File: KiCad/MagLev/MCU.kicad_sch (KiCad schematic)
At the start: 40 parts, among them J2 Programming header, J4 USB_B_Micro, Q16 TEMT7000X01, U6 ATmega328P-A, U8 FT232RL, U9 LM1117MP-5.0, Y3 J49SMH-16MHz

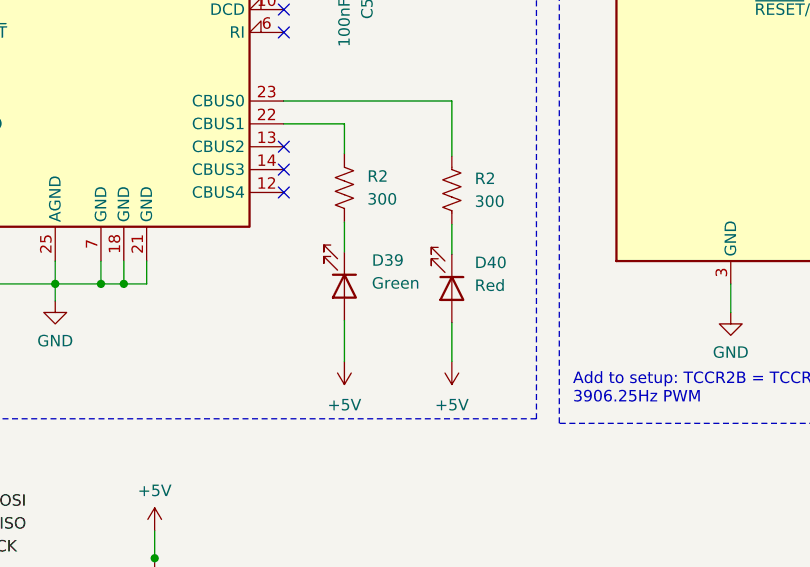
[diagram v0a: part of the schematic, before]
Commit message: Update BOM with JLCPCB PNs.
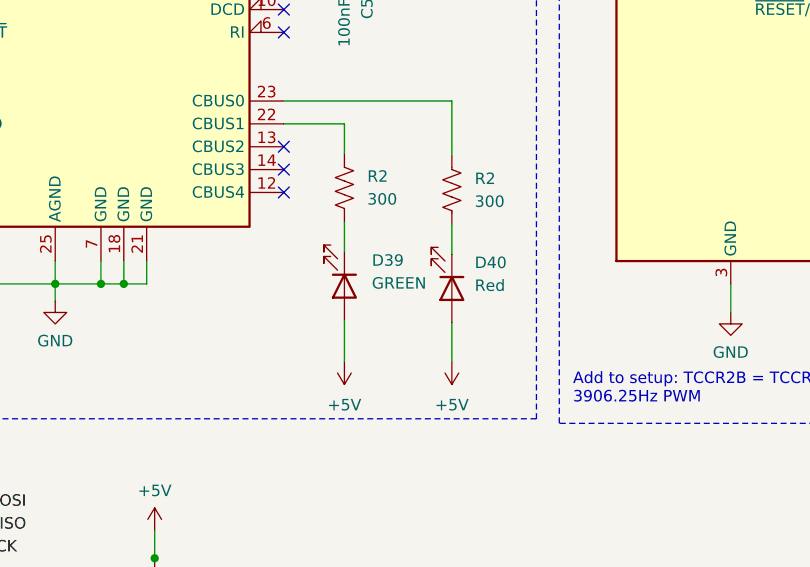
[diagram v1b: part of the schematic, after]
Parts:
- C5: JLC Part Number (none) -> C1804
- C5: JLC Part Number (none) -> C15850
- C5: JLC Part Number (none) -> C28233
- D28: JLC Part Number (none) -> C95872
- D39: value Green -> GREEN; JLC Part Number (none) -> C2297
- D40: JLC Part Number (none) -> C84256
- J2: JLC Part Number (none) -> C5142239
- J4: JLC Part Number (none) -> C428496
- R2: JLC Part Number (none) -> C17617
- R2: JLC Part Number (none) -> C17513
- R2: JLC Part Number (none) -> C17514
- R52: JLC Part Number (none) -> C3949945
- RESET1: JLC Part Number (none) -> C221877
- U6: JLC Part Number (none) -> C14877
- U8: JLC Part Number (none) -> C8690
- U9: JLC Part Number (none) -> C131933
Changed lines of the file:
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@@
       (effects (font (size 1.27 1.27)) hide)
     )
-    (property "JLC Part Number" "" (at 205.613 82.677 0)
+    (property "JLC Part Number" "C1804" (at 205.613 82.677 0)
       (effects (font (size 1.27 1.27)) hide)
     )
@@
       (effects (font (size 1.27 1.27)) hide)
     )
-    (property "JLC Part Number" "" (at 116.332 111.76 0)
+    (property "JLC Part Number" "C17617" (at 116.332 111.76 0)
       (effects (font (size 1.27 1.27)) hide)
     )
@@
       (effects (font (size 1.27 1.27)) hide)
     )
-    (property "JLC Part Number" "" (at 60.96 152.654 0)
+    (property "JLC Part Number" "C17513" (at 60.96 152.654 0)
       (effects (font (size 1.27 1.27)) hide)
     )
@@
       (effects (font (size 1.27 1.27)) hide)
     )
-    (property "JLC Part Number" "" (at 89.281 94.488 0)
+    (property "JLC Part Number" "C8690" (at 89.281 94.488 0)
       (effects (font (size 1.27 1.27)) hide)
     )
@@
       (effects (font (size 1.27 1.27)) hide)
     )
-    (property "JLC Part Number" "" (at 201.422 119.888 0)
+    (property "JLC Part Number" "C221877" (at 201.422 119.888 0)
       (effects (font (size 1.27 1.27)) hide)
     )
@@
       (effects (font (size 1.27 1.27)) hide)
     )
-    (property "JLC Part Number" "" (at 52.07 27.432 0)
+    (property "JLC Part Number" "C131933" (at 52.07 27.432 0)
       (effects (font (size 1.27 1.27)) hide)
     )
@@
       (effects (font (size 1.27 1.27)) hide)
     )
-    (property "JLC Part Number" "" (at 65.532 31.75 0)
+    (property "JLC Part Number" "C15850" (at 65.532 31.75 0)
       (effects (font (size 1.27 1.27)) hide)
     )
@@
       (effects (font (size 1.27 1.27)) hide)
     )
-    (property "JLC Part Number" "" (at 50.927 84.328 0)
+    (property "JLC Part Number" "C17513" (at 50.927 84.328 0)
       (effects (font (size 1.27 1.27)) hide)
     )
@@
       (effects (font (size 1.27 1.27)) hide)
     )
-    (property "JLC Part Number" "" (at 148.463 34.163 0)
+    (property "JLC Part Number" "C28233" (at 148.463 34.163 0)
       (effects (font (size 1.27 1.27)) hide)
     )
@@
       (effects (font (size 1.27 1.27)) hide)
     )
-    (property "JLC Part Number" "" (at 35.56 32.258 0)
+    (property "JLC Part Number" "C15850" (at 35.56 32.258 0)
       (effects (font (size 1.27 1.27)) hide)
     )
@@
       (effects (font (size 1.27 1.27)) hide)
     )
-    (property "JLC Part Number" "" (at 29.337 84.328 0)
+    (property "JLC Part Number" "C428496" (at 29.337 84.328 0)
       (effects (font (size 1.27 1.27)) hide)
     )
@@
       (effects (font (size 1.27 1.27)) hide)
     )
-    (property "JLC Part Number" "" (at 66.421 155.194 0)
+    (property "JLC Part Number" "C17513" (at 66.421 155.194 0)
       (effects (font (size 1.27 1.27)) hide)
     )
@@
       (effects (font (size 1.27 1.27)) hide)
     )
-    (property "JLC Part Number" "" (at 95.25 156.718 0)
+    (property "JLC Part Number" "C3949945" (at 95.25 156.718 0)
       (effects (font (size 1.27 1.27)) hide)
     )
@@
       (effects (font (size 1.27 1.27)) (justify left))
     )
-    (property "Value" "Green" (at 119.38 122.3645 90)
+    (property "Value" "GREEN" (at 119.38 122.3645 90)
       (effects (font (size 1.27 1.27)) (justify left))
     )
@@
       (effects (font (size 1.27 1.27)) hide)
     )
-    (property "JLC Part Number" "" (at 116.332 122.682 0)
+    (property "JLC Part Number" "C2297" (at 116.332 122.682 0)
       (effects (font (size 1.27 1.27)) hide)
     )
@@
       (effects (font (size 1.27 1.27)) hide)
     )
-    (property "JLC Part Number" "" (at 201.422 106.68 0)
+    (property "JLC Part Number" "C17513" (at 201.422 106.68 0)
       (effects (font (size 1.27 1.27)) hide)
     )
@@
       (effects (font (size 1.27 1.27)) hide)
     )
-    (property "JLC Part Number" "" (at 193.548 83.058 0)
+    (property "JLC Part Number" "C1804" (at 193.548 83.058 0)
       (effects (font (size 1.27 1.27)) hide)
     )
@@
       (effects (font (size 1.27 1.27)) hide)
     )
-    (property "JLC Part Number" "" (at 237.744 134.62 0)
+    (property "JLC Part Number" "C17514" (at 237.744 134.62 0)
       (effects (font (size 1.27 1.27)) hide)
     )
@@
       (effects (font (size 1.27 1.27)) hide)
     )
-    (property "JLC Part Number" "" (at 49.53 147.574 0)
+    (property "JLC Part Number" "C17513" (at 49.53 147.574 0)
       (effects (font (size 1.27 1.27)) hide)
     )
@@
       (effects (font (size 1.27 1.27)) hide)
     )
-    (property "JLC Part Number" "" (at 237.49 120.396 0)
+    (property "JLC Part Number" "C17514" (at 237.49 120.396 0)
       (effects (font (size 1.27 1.27)) hide)
     )
@@
       (effects (font (size 1.27 1.27)) hide)
     )
-    (property "JLC Part Number" "" (at 32.131 155.194 0)
+    (property "JLC Part Number" "C5142239" (at 32.131 155.194 0)
       (effects (font (size 1.27 1.27)) hide)
     )
@@
       (effects (font (size 1.27 1.27)) hide)
     )
-    (property "JLC Part Number" "" (at 98.044 62.484 0)
+    (property "JLC Part Number" "C28233" (at 98.044 62.484 0)
       (effects (font (size 1.27 1.27)) hide)
     )
@@
       (effects (font (size 1.27 1.27)) hide)
     )
-    (property "JLC Part Number" "" (at 57.277 86.868 0)
+    (property "JLC Part Number" "C17513" (at 57.277 86.868 0)
       (effects (font (size 1.27 1.27)) hide)
     )
@@
       (effects (font (size 1.27 1.27)) hide)
     )
-    (property "JLC Part Number" "" (at 66.167 67.183 0)
+    (property "JLC Part Number" "C28233" (at 66.167 67.183 0)
       (effects (font (size 1.27 1.27)) hide)
     )
@@
       (effects (font (size 1.27 1.27)) hide)
     )
-    (property "JLC Part Number" "" (at 117.602 86.868 0)
+    (property "JLC Part Number" "C28233" (at 117.602 86.868 0)
       (effects (font (size 1.27 1.27)) hide)
     )
@@
       (effects (font (size 1.27 1.27)) hide)
     )
-    (property "JLC Part Number" "" (at 159.258 84.328 0)
+    (property "JLC Part Number" "C14877" (at 159.258 84.328 0)
       (effects (font (size 1.27 1.27)) hide)
     )
@@
       (effects (font (size 1.27 1.27)) hide)
     )
-    (property "JLC Part Number" "" (at 237.744 127.508 0)
+    (property "JLC Part Number" "C17514" (at 237.744 127.508 0)
       (effects (font (size 1.27 1.27)) hide)
     )
@@
       (effects (font (size 1.27 1.27)) hide)
     )
-    (property "JLC Part Number" "" (at 128.27 112.014 0)
+    (property "JLC Part Number" "C17617" (at 128.27 112.014 0)
       (effects (font (size 1.27 1.27)) hide)
     )
@@
       (effects (font (size 1.27 1.27)) hide)
     )
-    (property "JLC Part Number" "" (at 128.27 122.936 0)
+    (property "JLC Part Number" "C84256" (at 128.27 122.936 0)
       (effects (font (size 1.27 1.27)) hide)
     )
@@
       (effects (font (size 1.27 1.27)) hide)
     )
-    (property "JLC Part Number" "" (at 55.118 150.114 0)
+    (property "JLC Part Number" "C17513" (at 55.118 150.114 0)
       (effects (font (size 1.27 1.27)) hide)
     )
@@
       (effects (font (size 1.27 1.27)) hide)
     )
-    (property "JLC Part Number" "" (at 41.275 61.214 0)
-      (effects (font (size 1.27 1.27)) hide)
-    )
+    (property "JLC Part Number" "C95872" (at 41.275 61.214 0)
+      (effects (font (size 1.27 1.27)) hide)
+    )

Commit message: Add board art folder and upload svg files.
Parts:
- R2: JLC Part Number C17514 -> (none)
- R52: JLC Part Number C3949945 -> C27834
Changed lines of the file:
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@@
       (effects (font (size 1.27 1.27)) hide)
     )
-    (property "JLC Part Number" "C3949945" (at 95.25 156.718 0)
+    (property "JLC Part Number" "C27834" (at 95.25 156.718 0)
       (effects (font (size 1.27 1.27)) hide)
     )
@@
       (effects (font (size 1.27 1.27)) hide)
     )
-    (property "JLC Part Number" "C17514" (at 237.744 134.62 0)
+    (property "JLC Part Number" "" (at 237.744 134.62 0)
       (effects (font (size 1.27 1.27)) hide)
     )
@@
       (effects (font (size 1.27 1.27)) hide)
     )
-    (property "JLC Part Number" "C17514" (at 237.49 120.396 0)
+    (property "JLC Part Number" "" (at 237.49 120.396 0)
       (effects (font (size 1.27 1.27)) hide)
     )
@@
       (effects (font (size 1.27 1.27)) hide)
     )
-    (property "JLC Part Number" "C17514" (at 237.744 127.508 0)
-      (effects (font (size 1.27 1.27)) hide)
-    )
+    (property "JLC Part Number" "" (at 237.744 127.508 0)
+      (effects (font (size 1.27 1.27)) hide)
+    )

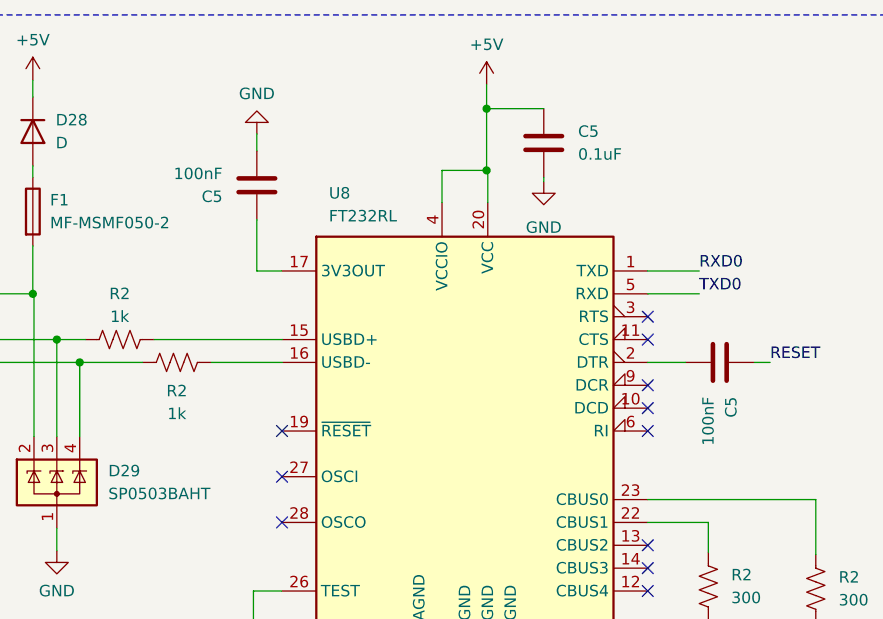
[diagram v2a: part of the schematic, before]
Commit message: Create project outputs for order, cleanup BOM.
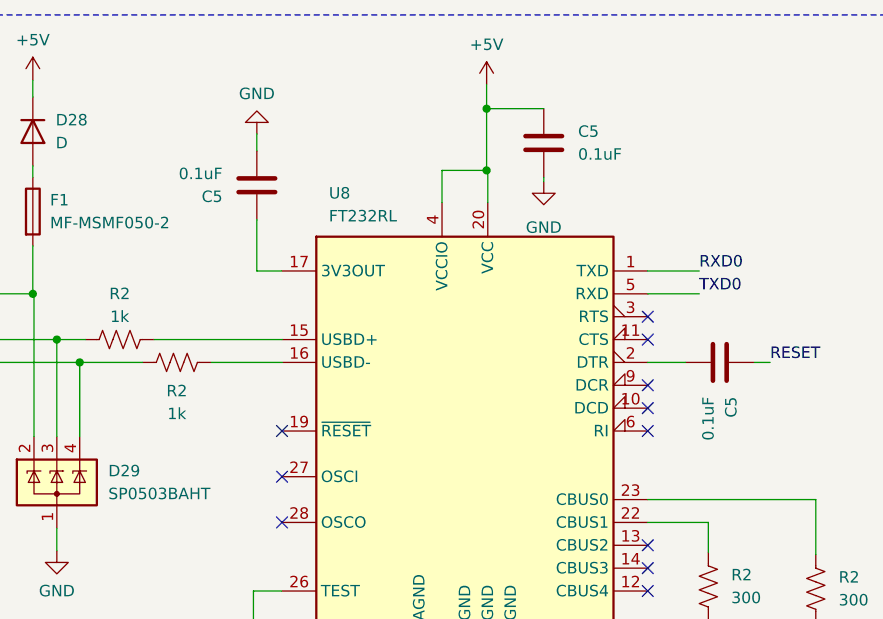
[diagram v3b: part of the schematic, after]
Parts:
- C5: value 100nF -> 0.1uF
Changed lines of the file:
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@@
       (effects (font (size 1.27 1.27)) (justify left))
     )
-    (property "Value" "100nF" (at 62.357 65.913 0)
+    (property "Value" "0.1uF" (at 62.357 65.913 0)
       (effects (font (size 1.27 1.27)) (justify left))
     )
@@
       (effects (font (size 1.27 1.27)) (justify left))
     )
-    (property "Value" "100nF" (at 116.332 90.678 0)
+    (property "Value" "0.1uF" (at 116.332 90.678 0)
       (effects (font (size 1.27 1.27)) (justify left))
     )
